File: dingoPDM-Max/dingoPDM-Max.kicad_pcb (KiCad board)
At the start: 4 copper layers, 72.4 x 95.2 mm, 136 parts, among them J1 RedCubeTerminal, J2 USB_C_Receptacle_USB2.0, J3 RedCubeTerminal, J4 Conn_01x12, J5 TC, SW1 BOOT, U1 VXO780x-500-M, U10 BTS70015-1ESP, U11 BTS70015-1ESP, U2 LD1117S33CTR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

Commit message: add dc-dc options and 5v cap
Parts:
- added C39: 100uF, Capacitor_SMD:CP_Elec_6.3x7.7, F.Cu at (-30.0, 56.6)
- added U12: OKI-78SR-5_1.5-W36H-C, Converter_DCDC:Converter_DCDC_Murata_OKI-78SR_Horizontal, F.Cu at (-19.2, 39.6)
- added U13: TSR_1-2450, Converter_DCDC:Converter_DCDC_TRACO_TSR-1_THT, F.Cu at (-26.7, 39.6)
- U10, U11, U8, U9: value BTS70015-1ESP -> BTS70012-1ESP
- moved D4 4.33 mm to (-29.2, 51.6)
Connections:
- net Net-(D3-K) renamed +12P
- net Net-(D4-A) renamed +5VP
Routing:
- net +5VP: track 9.52 -> 23.0 mm
- net +12P: track 3.02 -> 13.0 mm
- net +5V: track 152.8 -> 156.9 mm
- net GND: vias 63 -> 69
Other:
- board text added: "dingoPDM-Max v1.1"
- board text removed: "dingoPDM-Max v1.0"

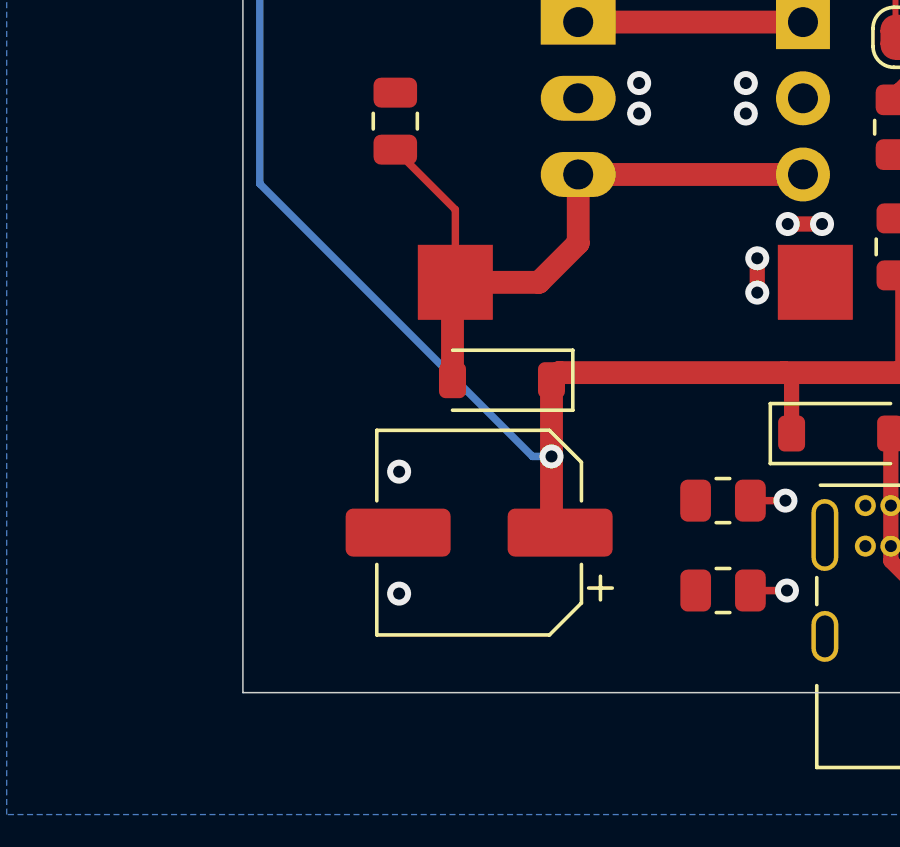
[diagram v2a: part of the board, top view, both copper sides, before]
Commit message: switch to ceramic caps
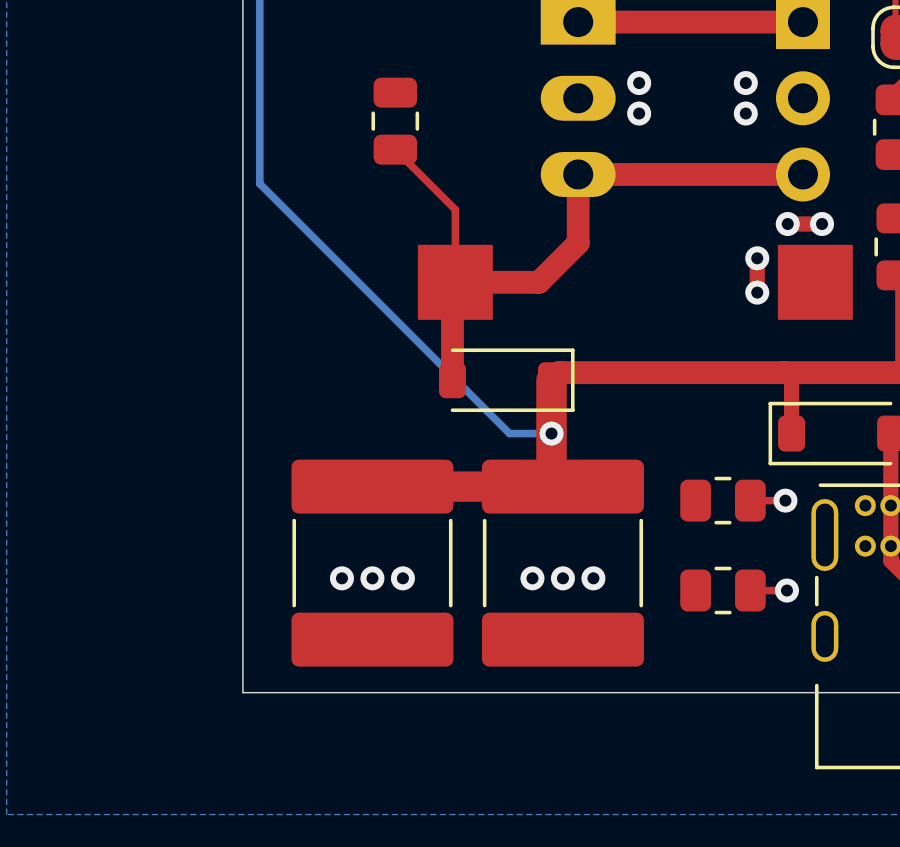
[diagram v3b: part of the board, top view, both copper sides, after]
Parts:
- added C40: 47uF, Capacitor_SMD:C_2220_5750Metric, F.Cu at (-27.2, 57.7)
- C39: value 100uF -> 47uF; footprint Capacitor_SMD:CP_Elec_6.3x7.7 -> Capacitor_SMD:C_2220_5750Metric
- moved C39 3.70 mm to (-33.5, 57.7), turned to -90 degrees
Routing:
- net +5V: track 156.9 -> 161.4 mm
- net GND: vias 69 -> 73

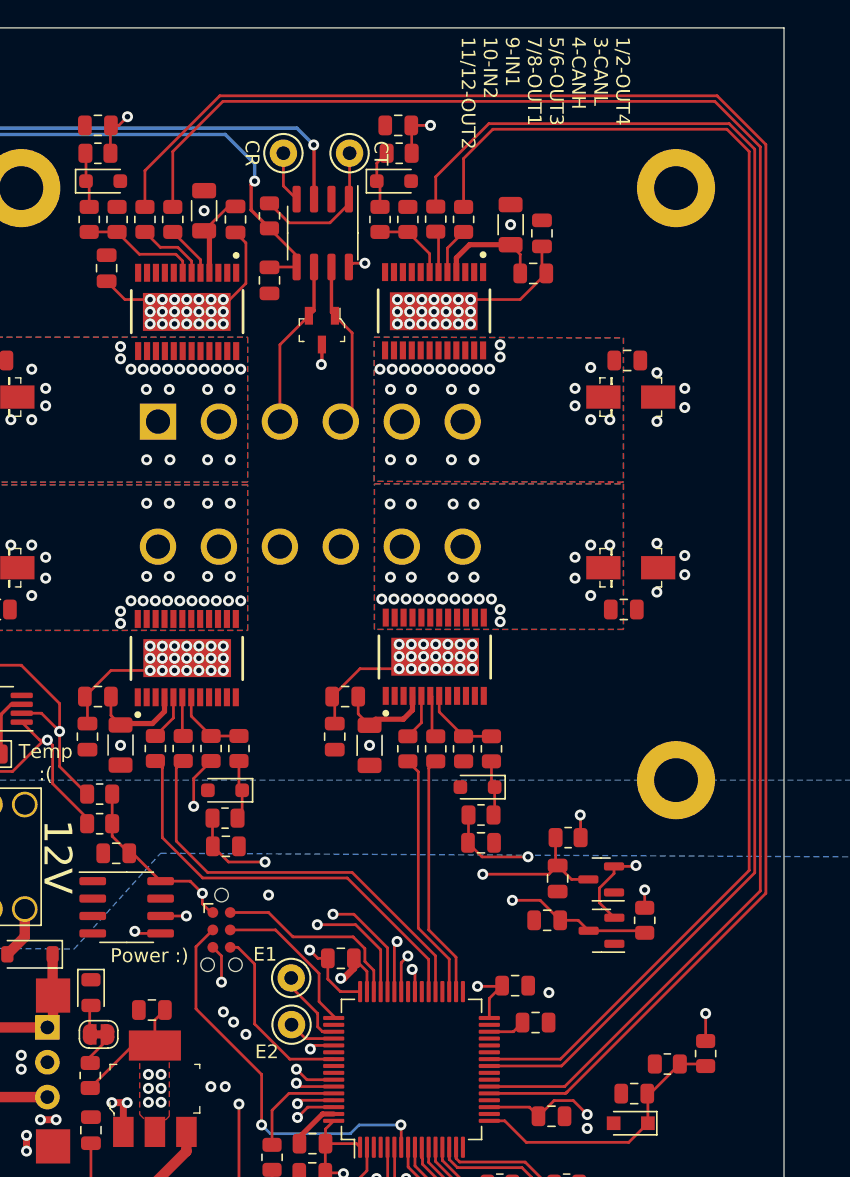
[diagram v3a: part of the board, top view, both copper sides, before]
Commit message: fixed bad zone, shifted traces, increase trace widths
update part numbers for ibom
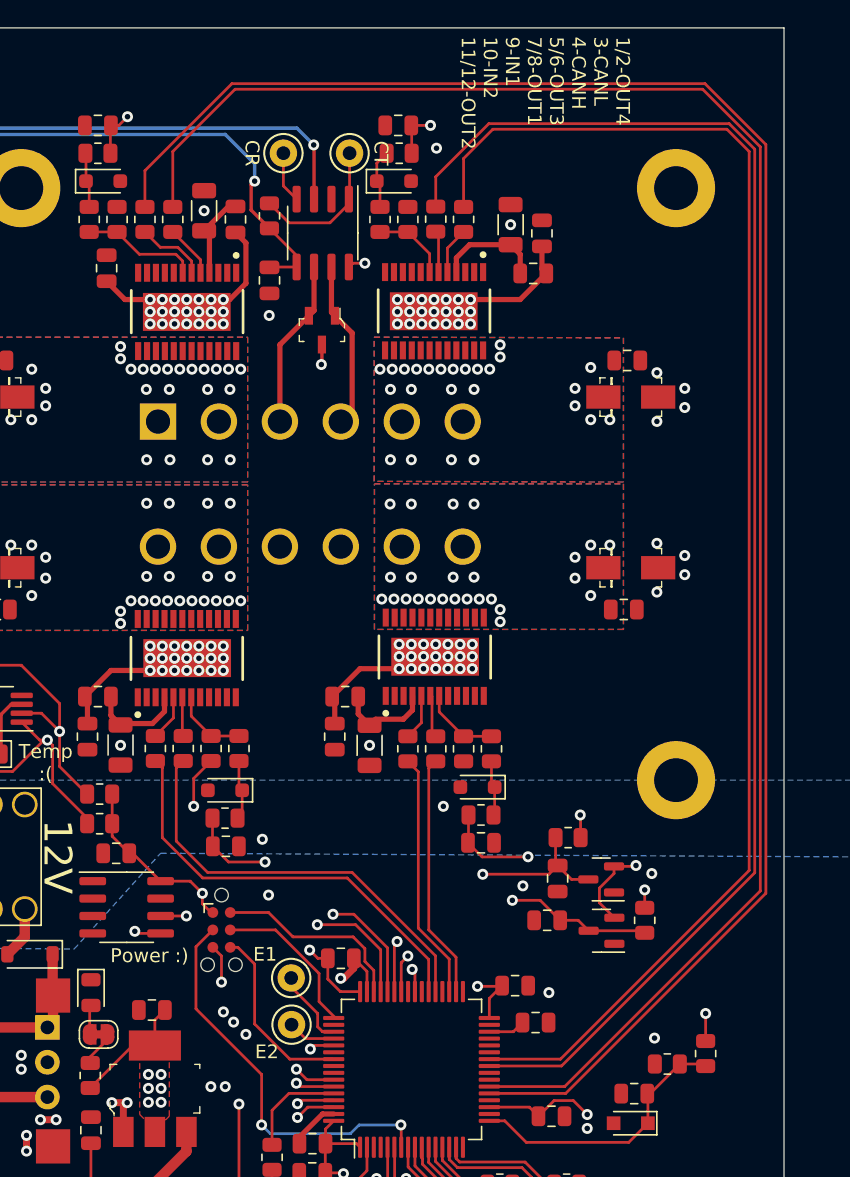
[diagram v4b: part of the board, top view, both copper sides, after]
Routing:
- net PF_IN4: track 129.7 -> 130.4 mm
- net PF_DEN4: track 132.5 -> 133.2 mm
- net GND: vias 73 -> 80
